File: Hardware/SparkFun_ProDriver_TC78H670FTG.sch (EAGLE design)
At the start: 43 parts, among them J1 POWER_JACKTOE, J2 LATCH, J3 PTH, J4 LATCH, J5 LATCH, J6 PTH, J7 LATCH, J8 PTH, U1 TC78H670FTG

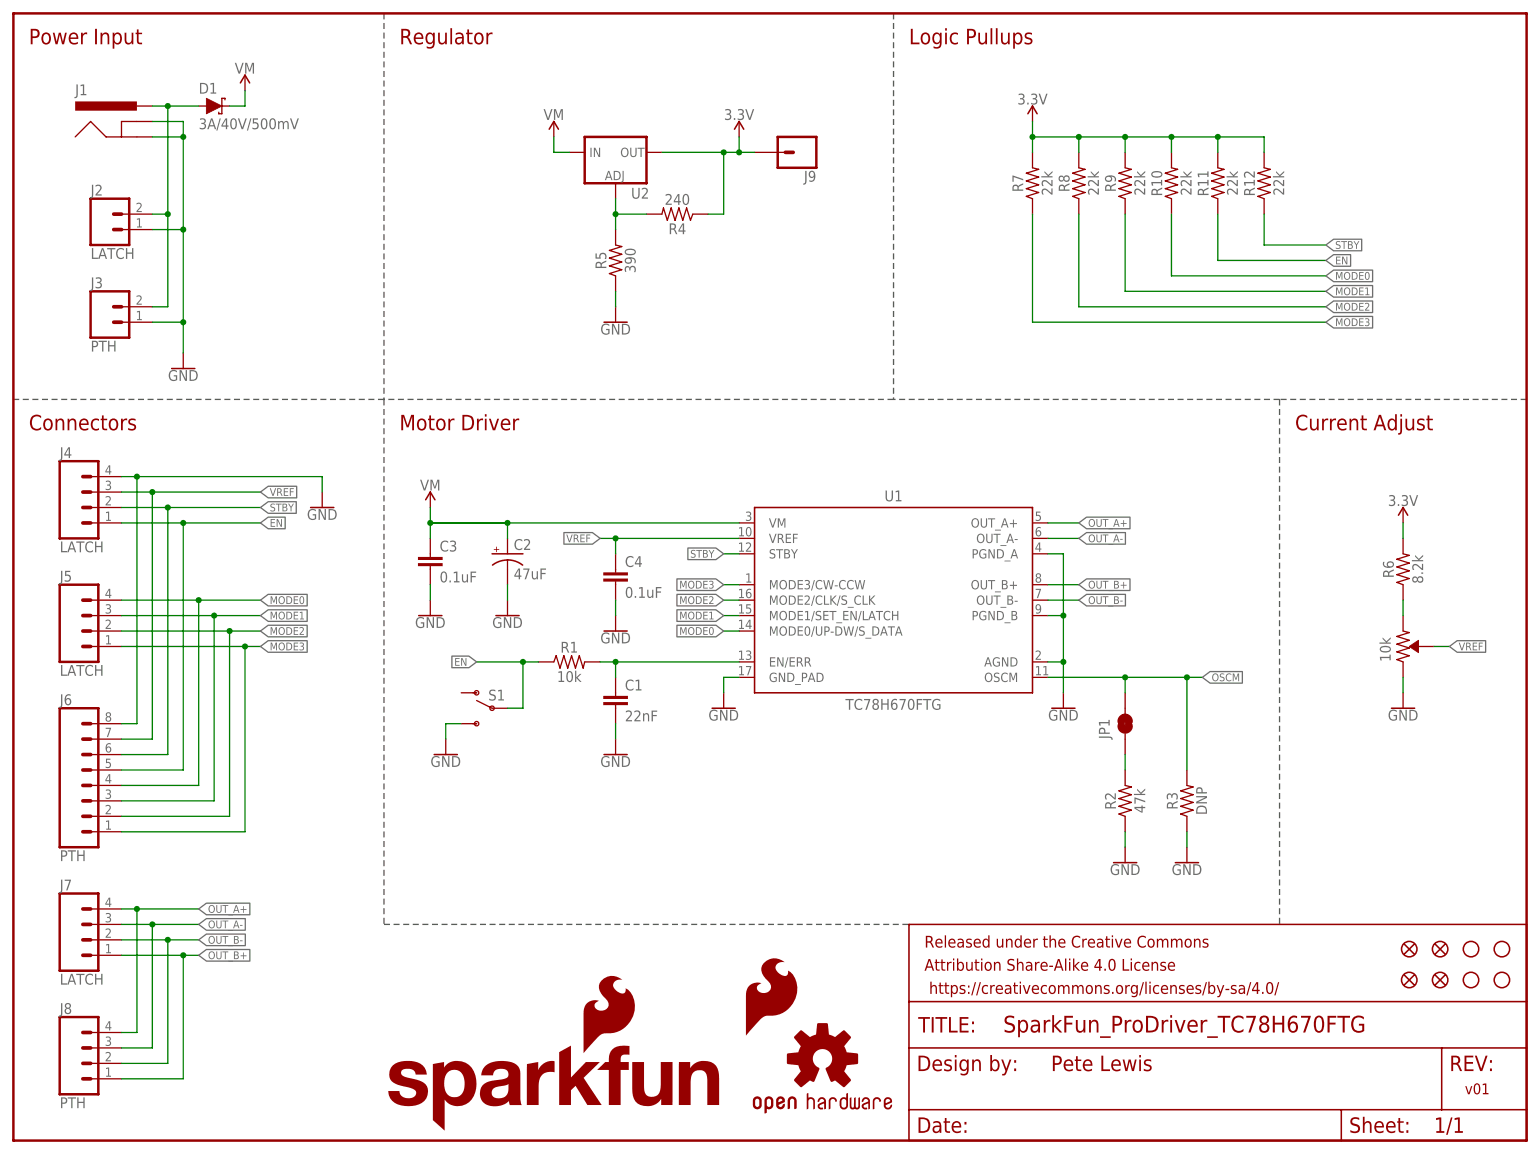
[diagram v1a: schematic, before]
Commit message: Corrected EN/ERR pin access
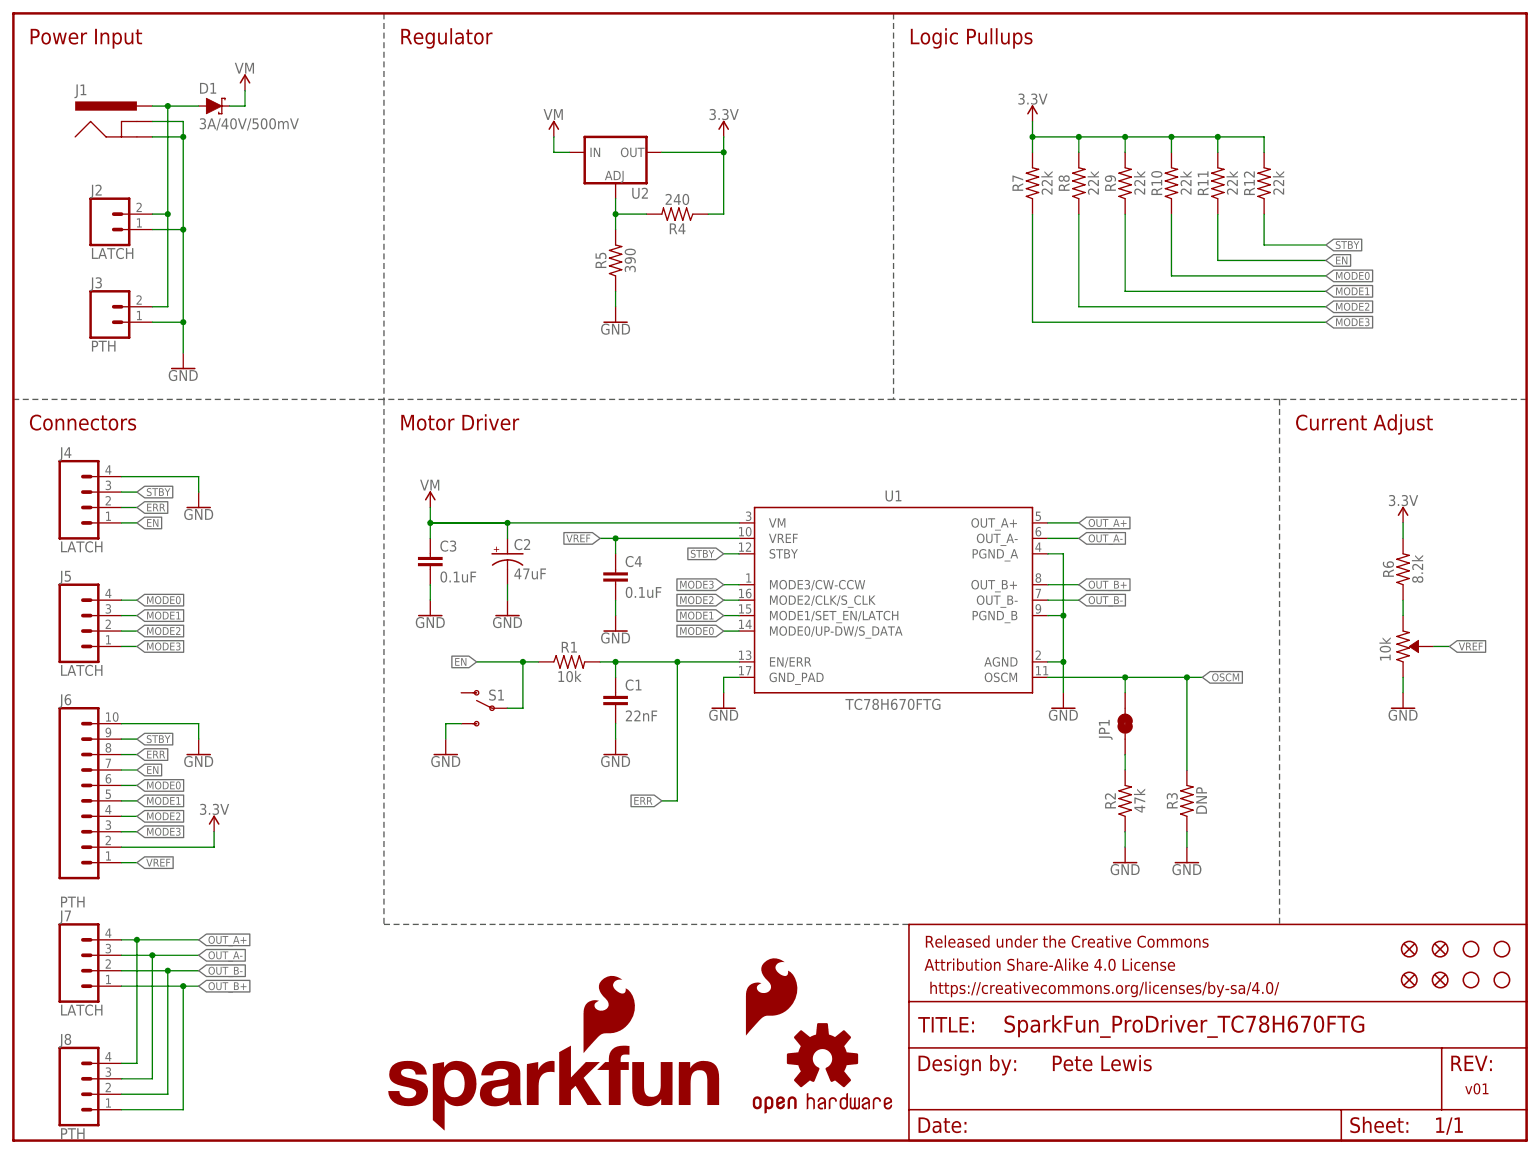
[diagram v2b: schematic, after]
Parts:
- removed J9: (no value), SparkFun-Connectors:CONN_01PTH_NO_SILK_YES_STOP
- J6: device SparkFun-Connectors:CONN_08NO_SILK_FEMALE_PTH -> SparkFun-Connectors:CONN_10NO_SILK_PTH_FEMALE
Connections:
- removed net N$1: C1.1, R1.2, U1.EN/ERR
- new net ERR: C1.1, J4.2, J6.8, R1.2, U1.EN/ERR
- net 3.3V: now also J6.2; no longer J9.1
- net EN: now also J6.7; no longer J6.5
- net GND: now also J6.10; no longer J6.8
- net MODE0: now also J6.6; no longer J6.4
- net MODE1: now also J6.5; no longer J6.3
- net MODE2: now also J6.4; no longer J6.2
- net MODE3: now also J6.3; no longer J6.1
- net STBY: now also J4.3, J6.9; no longer J4.2, J6.6
- net VREF: now also J6.1; no longer J4.3, J6.7
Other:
- moved on the sheet: J7, J8
